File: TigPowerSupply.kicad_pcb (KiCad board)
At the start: 2 copper layers, 86.4 x 34.3 mm, 10 parts, among them J1 Screw_Terminal_01x02, J2 Conn_01x03, U1 MCP1826S

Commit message: tweaked the dimensions to be round mm values
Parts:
- moved J1 5.32 mm to (78.7, 54.5), turned to -90 degrees
- moved C2 2.90 mm to (138.2, 58.4)
- moved PS1 2.90 mm to (91.6, 54.6)
- moved J2 2.90 mm to (149.8, 62.0)
- moved C1 2.90 mm to (131.8, 58.4)
- moved U1 2.90 mm to (132.1, 49.5)
- moved H2 2.60 mm to (76.4, 68.7)
- moved H4 2.54 mm to (151.4, 68.7)
- moved H3 2.38 mm to (151.4, 43.7)
- moved H1 0.79 mm to (77.4, 43.7)
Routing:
- net Net-(J1-Pin_2): track 19.8 -> 13.0 mm
- net Net-(J1-Pin_1): track 10.4 -> 13.0 mm
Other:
- board size 86.4 x 34.3 mm -> 85 x 34 mm
- board text added: "JLCJLCJLCJLC"

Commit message: bla
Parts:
- H1, H2, H3, H4: footprint MountingHole:MountingHole_2.2mm_M2_DIN965 -> MountingHole:MountingHole_3.2mm_M3_DIN965
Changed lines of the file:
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@@
 		)
 	)
-	(footprint "MountingHole:MountingHole_2.2mm_M2_DIN965"
+	(footprint "MountingHole:MountingHole_3.2mm_M3_DIN965"
 		(layer "F.Cu")
 		(at 151.43 68.66)
-		(descr "Mounting Hole 2.2mm, no annular, M2, DIN965")
-		(tags "mounting hole 2.2mm no annular m2 din965")
+		(descr "Mounting Hole 3.2mm, no annular, M3, DIN965")
+		(tags "mounting hole 3.2mm no annular m3 din965")
 		(property "Reference" "H4"
-			(at 0 -2.9 0)
+			(at 0 -3.8 0)
 			(layer "F.SilkS")
 			(hide yes)
@@
 		)
 		(property "Value" "MountingHole"
-			(at 0 2.9 0)
+			(at 0 3.8 0)
 			(layer "F.Fab")
 			(effects
@@
 			)
 		)
-		(property "Footprint" "MountingHole:MountingHole_2.2mm_M2_DIN965"
+		(property "Footprint" "MountingHole:MountingHole_3.2mm_M3_DIN965"
 			(at 0 0 0)
 			(unlocked yes)
@@
 		(fp_circle
 			(center 0 0)
-			(end 1.9 0)
+			(end 2.8 0)
 			(stroke
 				(width 0.15)
@@
 		(fp_circle
 			(center 0 0)
-			(end 2.15 0)
+			(end 3.05 0)
 			(stroke
 				(width 0.05)
@@
 		(pad "" np_thru_hole circle
 			(at 0 0)
-			(size 2.2 2.2)
-			(drill 2.2)
+			(size 3.2 3.2)
+			(drill 3.2)
 			(layers "*.Cu" "*.Mask")
 		)
@@
 		)
 	)
-	(footprint "MountingHole:MountingHole_2.2mm_M2_DIN965"
+	(footprint "MountingHole:MountingHole_3.2mm_M3_DIN965"
 		(layer "F.Cu")
 		(at 77.43 43.66)
-		(descr "Mounting Hole 2.2mm, no annular, M2, DIN965")
-		(tags "mounting hole 2.2mm no annular m2 din965")
+		(descr "Mounting Hole 3.2mm, no annular, M3, DIN965")
+		(tags "mounting hole 3.2mm no annular m3 din965")
 		(property "Reference" "H1"
-			(at 0 -2.9 0)
+			(at 0 -3.8 0)
 			(layer "F.SilkS")
 			(hide yes)
@@
 		)
 		(property "Value" "MountingHole"
-			(at 0 2.9 0)
+			(at 0 3.8 0)
 			(layer "F.Fab")
 			(effects
@@
 			)
 		)
-		(property "Footprint" "MountingHole:MountingHole_2.2mm_M2_DIN965"
+		(property "Footprint" "MountingHole:MountingHole_3.2mm_M3_DIN965"
 			(at 0 0 0)
 			(unlocked yes)
@@
 		(fp_circle
 			(center 0 0)
-			(end 1.9 0)
+			(end 2.8 0)
 			(stroke
 				(width 0.15)
@@
 		(fp_circle
 			(center 0 0)
-			(end 2.15 0)
+			(end 3.05 0)
 			(stroke
 				(width 0.05)
@@
 		)
 		(fp_text user "${REFERENCE}"
-			(at 2 0 0)
+			(at 0 0 0)
 			(layer "F.Fab")
 			(effects
@@
 		(pad "" np_thru_hole circle
 			(at 0 0)
-			(size 2.2 2.2)
-			(drill 2.2)
+			(size 3.2 3.2)
+			(drill 3.2)
 			(layers "*.Cu" "*.Mask")
 		)
 	)
-	(footprint "MountingHole:MountingHole_2.2mm_M2_DIN965"
+	(footprint "MountingHole:MountingHole_3.2mm_M3_DIN965"
 		(layer "F.Cu")
 		(at 151.43 43.66)
-		(descr "Mounting Hole 2.2mm, no annular, M2, DIN965")
-		(tags "mounting hole 2.2mm no annular m2 din965")
+		(descr "Mounting Hole 3.2mm, no annular, M3, DIN965")
+		(tags "mounting hole 3.2mm no annular m3 din965")
 		(property "Reference" "H3"
-			(at 0 -2.9 0)
+			(at 0 -3.8 0)
 			(layer "F.SilkS")
 			(hide yes)
@@
 		)
 		(property "Value" "MountingHole"
-			(at 0 2.9 0)
+			(at 0 3.8 0)
 			(layer "F.Fab")
 			(effects
@@
 			)
 		)
-		(property "Footprint" "MountingHole:MountingHole_2.2mm_M2_DIN965"
+		(property "Footprint" "MountingHole:MountingHole_3.2mm_M3_DIN965"
 			(at 0 0 0)
 			(unlocked yes)
@@
 		(fp_circle
 			(center 0 0)
-			(end 1.9 0)
+			(end 2.8 0)
 			(stroke
 				(width 0.15)
@@
 		(fp_circle
 			(center 0 0)
-			(end 2.15 0)
+			(end 3.05 0)
 			(stroke
 				(width 0.05)
@@
 		)
 		(fp_text user "${REFERENCE}"
-			(at -1 -1 0)
+			(at 0 0 0)
 			(layer "F.Fab")
 			(effects
@@
 		(pad "" np_thru_hole circle
 			(at 0 0)
-			(size 2.2 2.2)
-			(drill 2.2)
+			(size 3.2 3.2)
+			(drill 3.2)
 			(layers "*.Cu" "*.Mask")
 		)
 	)
-	(footprint "MountingHole:MountingHole_2.2mm_M2_DIN965"
+	(footprint "MountingHole:MountingHole_3.2mm_M3_DIN965"
 		(layer "F.Cu")
 		(at 76.43 68.66)
-		(descr "Mounting Hole 2.2mm, no annular, M2, DIN965")
-		(tags "mounting hole 2.2mm no annular m2 din965")
+		(descr "Mounting Hole 3.2mm, no annular, M3, DIN965")
+		(tags "mounting hole 3.2mm no annular m3 din965")
 		(property "Reference" "H2"
-			(at 0 -2.9 0)
+			(at 0 -3.8 0)
 			(layer "F.SilkS")
 			(hide yes)
@@
 		)
 		(property "Value" "MountingHole"
-			(at 0 2.9 0)
+			(at 0 3.8 0)
 			(layer "F.Fab")
 			(effects
@@
 			)
 		)
-		(property "Footprint" "MountingHole:MountingHole_2.2mm_M2_DIN965"
+		(property "Footprint" "MountingHole:MountingHole_3.2mm_M3_DIN965"
 			(at 0 0 0)
 			(unlocked yes)
@@
 		(fp_circle
 			(center 0 0)
-			(end 1.9 0)
+			(end 2.8 0)
 			(stroke
 				(width 0.15)
@@
 		(fp_circle
 			(center 0 0)
-			(end 2.15 0)
+			(end 3.05 0)
 			(stroke
 				(width 0.05)
@@
 		(pad "" np_thru_hole circle
 			(at 0 0)
-			(size 2.2 2.2)
-			(drill 2.2)
+			(size 3.2 3.2)
+			(drill 3.2)
 			(layers "*.Cu" "*.Mask")
 		)
@@
 		)
 	)
+	(dimension
+		(type aligned)
+		(layer "Dwgs.User")
+		(pts
+			(xy 151.43 68.66) (xy 151.43 43.66)
+		)
+		(height 18.17)
+		(gr_text "25.0000 mm"
+			(at 168.45 56.16 90)
+			(layer "Dwgs.User")
+			(effects
+				(font
+					(size 1 1)
+					(thickness 0.15)
+				)
+			)
+		)
+		(format
+			(prefix "")
+			(suffix "")
+			(units 3)
+			(units_format 1)
+			(precision 4)
+		)
+		(style
+			(thickness 0.1)
+			(arrow_length 1.27)
+			(text_position_mode 0)
+			(extension_height 0.58642)
+			(extension_offset 0.5) keep_text_aligned)
+	)
+	(dimension
+		(type aligned)
+		(layer "Dwgs.User")
+		(pts
+			(xy 76.43 68.66) (xy 151.43 68.66)
+		)
+		(height 14.14)
+		(gr_text "75.0000 mm"
+			(at 113.93 81.65 0)
+			(layer "Dwgs.User")
+			(effects
+				(font
+					(size 1 1)
+					(thickness 0.15)
+				)
+			)
+		)
+		(format
+			(prefix "")
+			(suffix "")
+			(units 3)
+			(units_format 1)
+			(precision 4)
+		)
+		(style
+			(thickness 0.1)
+			(arrow_length 1.27)
+			(text_position_mode 0)
+			(extension_height 0.58642)
+			(extension_offset 0.5) keep_text_aligned)
+	)
 	(segment

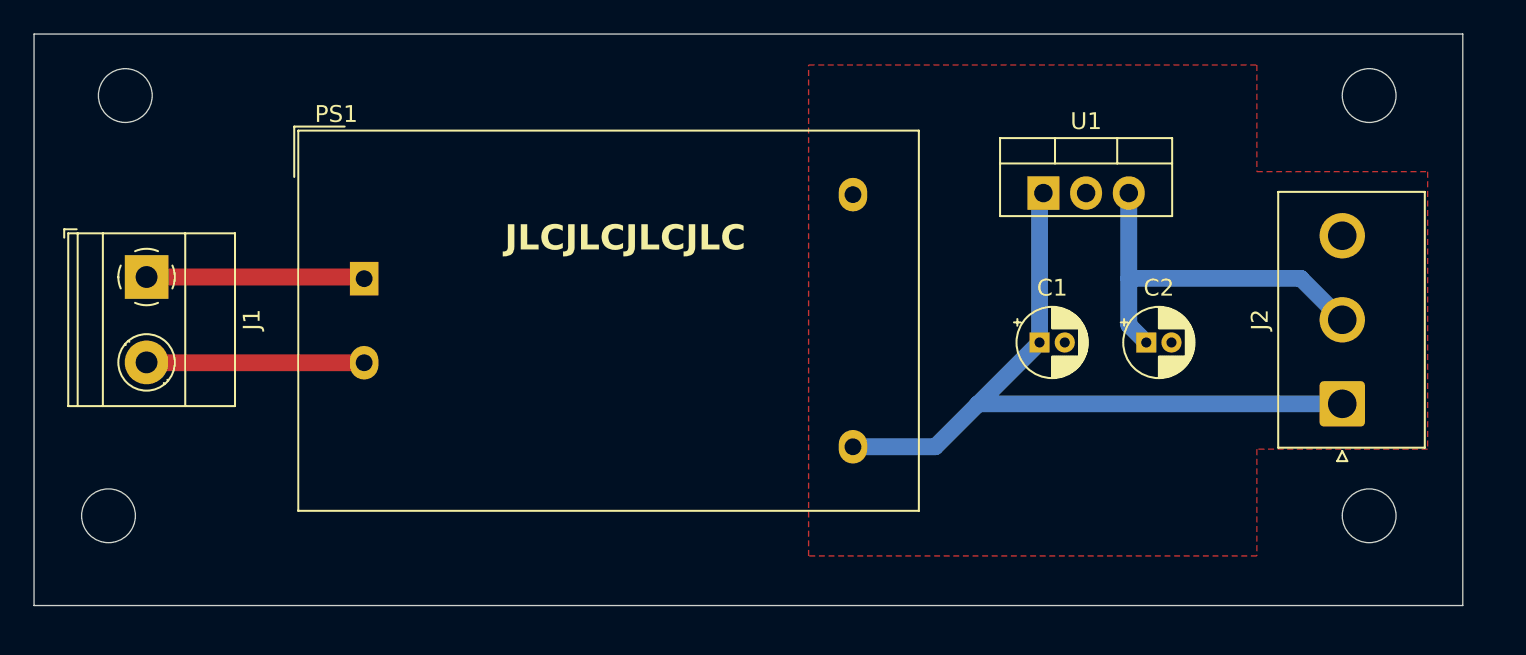
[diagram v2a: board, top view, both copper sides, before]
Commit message: moved regulator and changed output connector
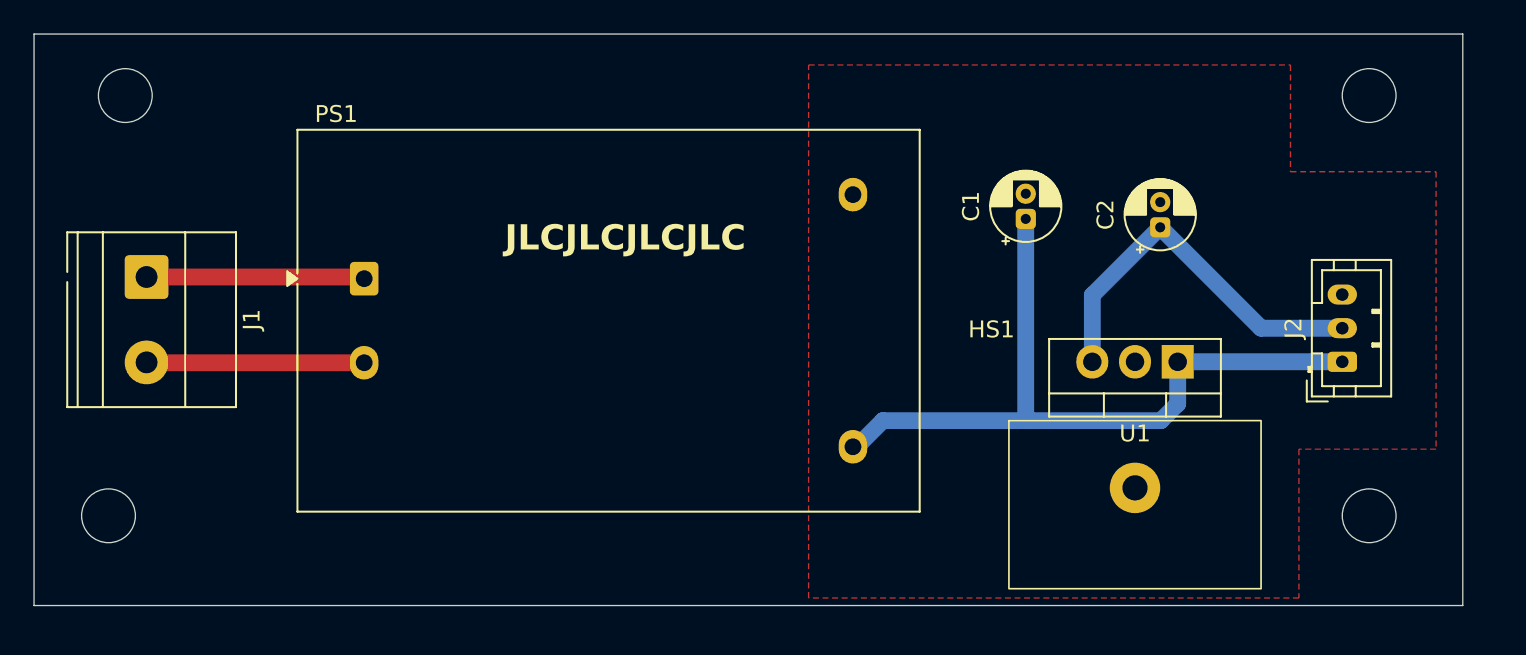
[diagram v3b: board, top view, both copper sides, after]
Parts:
- added HS1: Heatsink_Pad, GJ_HeatSink:Heatsink_10x15x40_TTO220, F.Cu at (137.5, 67.0)
- J2: footprint Connector_JST:JST_NV_B03P-NV_1x03_P5.00mm_Vertical -> Connector_JST:JST_PH_B3B-PH-K_1x03_P2.00mm_Vertical
- moved U1 12.8 mm to (140.0, 59.5), turned to 180 degrees
- moved C1 7.40 mm to (131.0, 51.0), turned to 90 degrees
- moved C2 6.90 mm to (139.0, 51.5), turned to 90 degrees
- moved J2 2.50 mm to (149.8, 59.5)
